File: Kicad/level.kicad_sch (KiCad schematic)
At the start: 38 parts, among them Q1 2N7002, Q10 MMBT5551L, Q11 2N7002, Q12 2N7002, Q2 2N7002, Q3 AO3401A, Q4 MMBT5551L, Q5 2N7002, Q6 2N7002, Q7 AO3401A, Q8 2N7002, Q9 2N7002, SW2 TEST_1, SW3 TEST_2

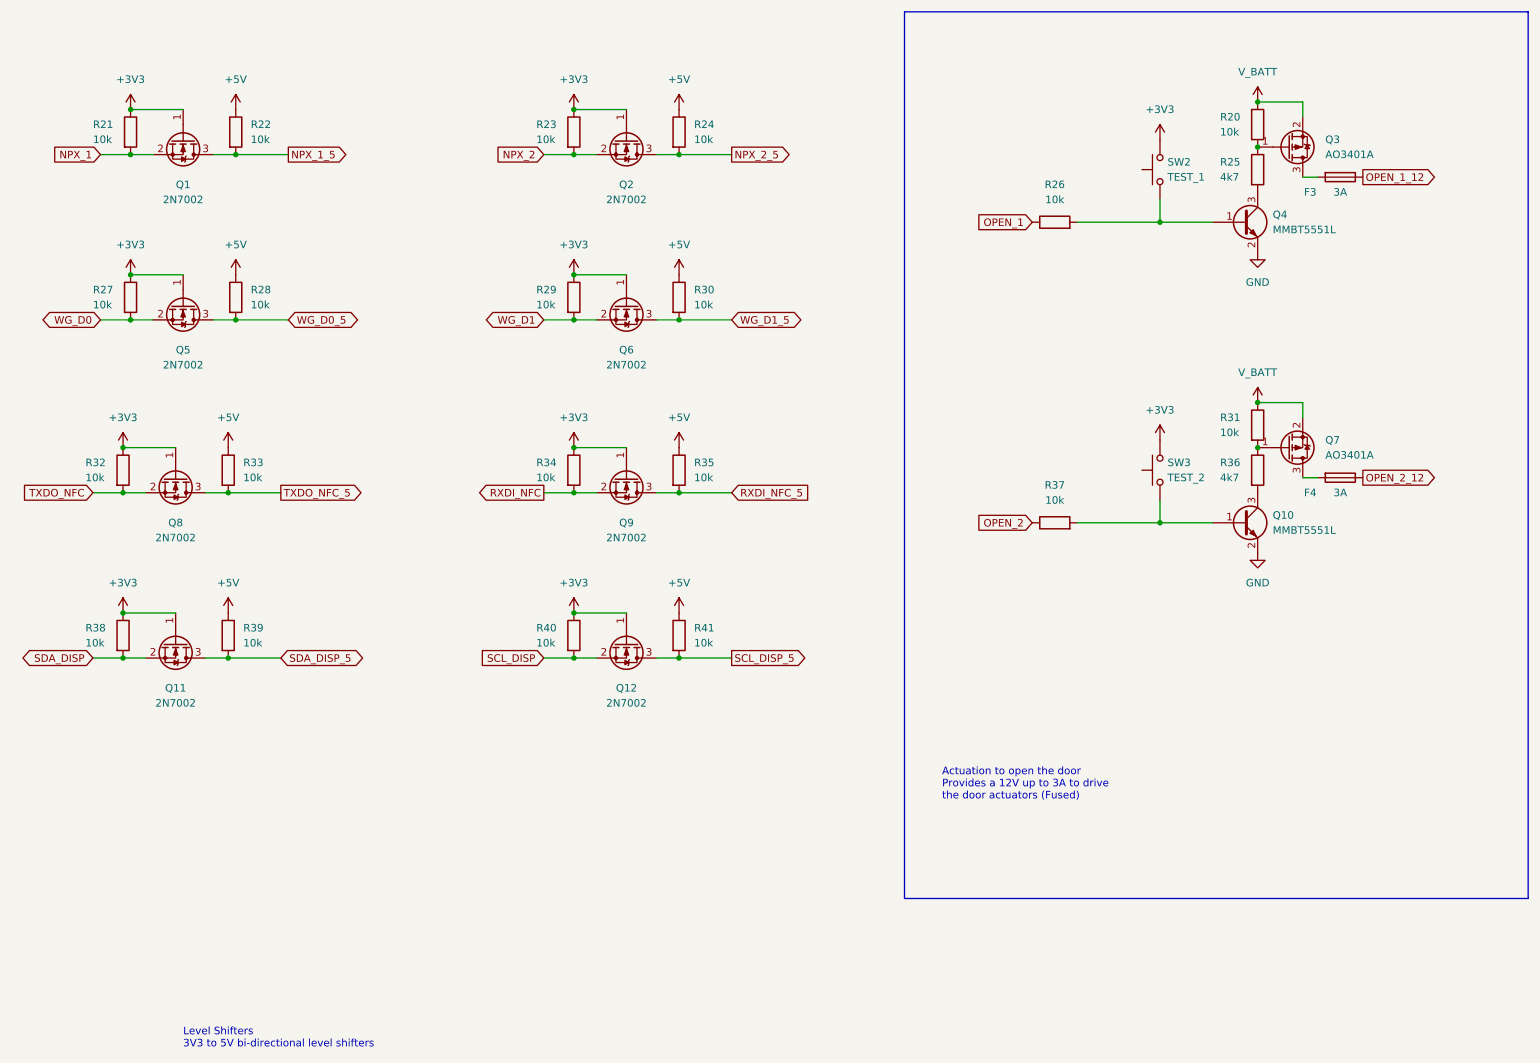
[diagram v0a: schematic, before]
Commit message: Rework of power circuits to improve protection
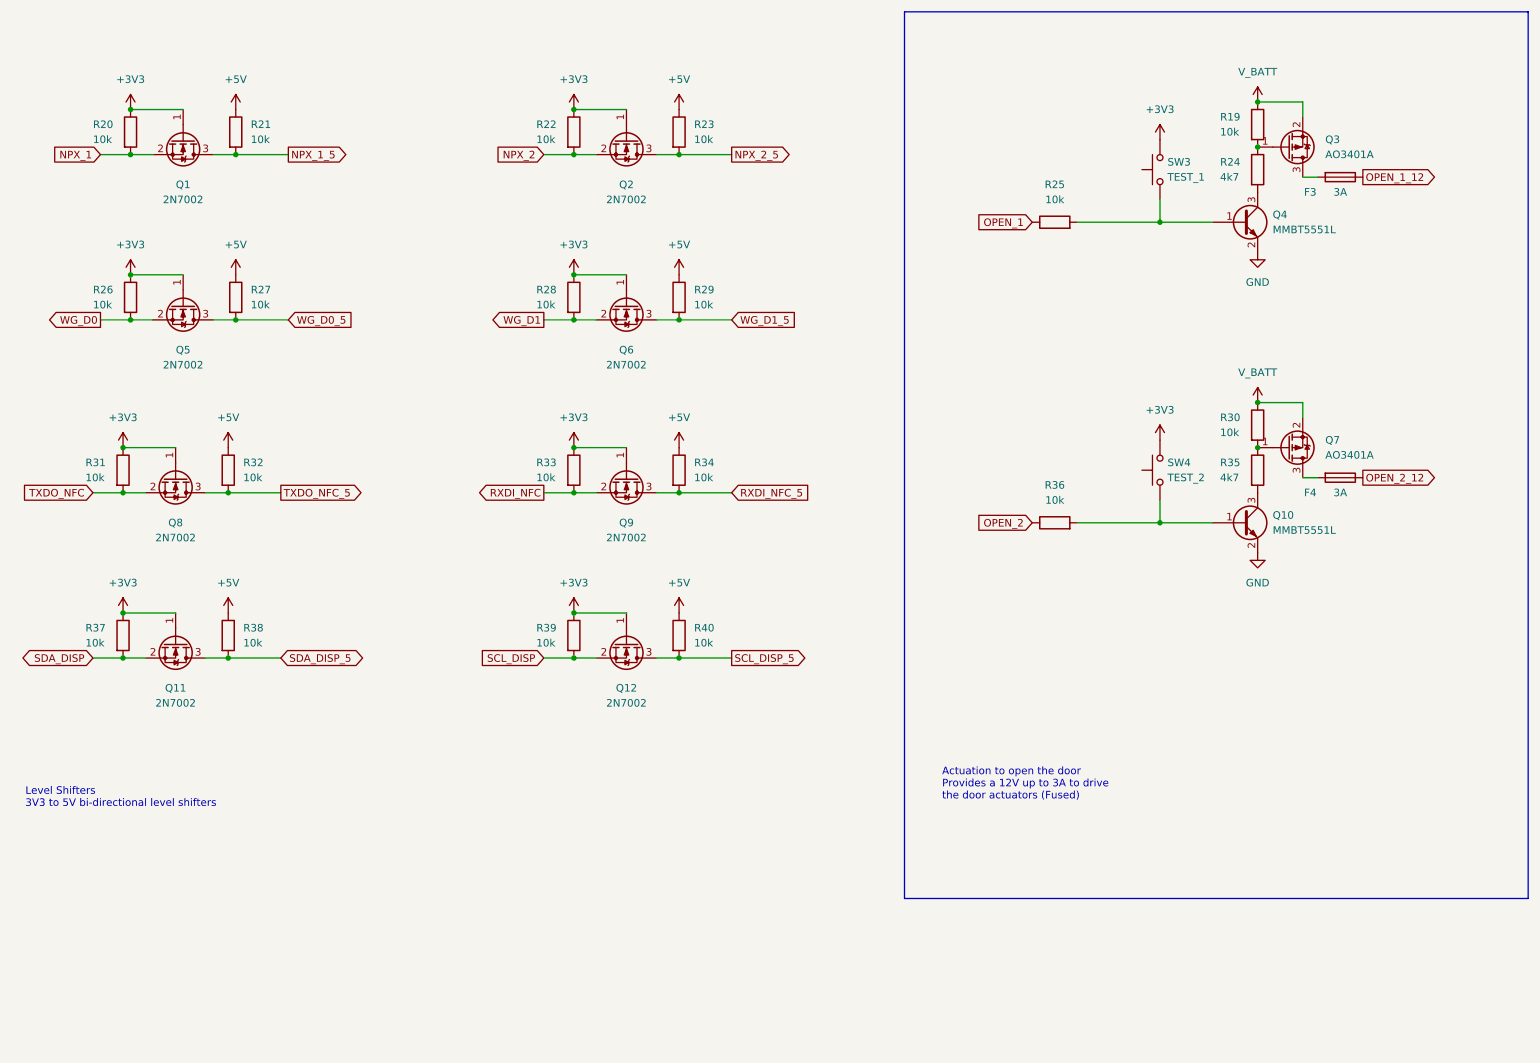
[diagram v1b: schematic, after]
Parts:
- renumbered R20 to R19, R21 to R20, R22 to R21, R23 to R22, R24 to R23, R25 to R24, R26 to R25, R27 to R26, R28 to R27, R29 to R28, R30 to R29, R31 to R30, R32 to R31, R33 to R32, R34 to R33, R35 to R34, R36 to R35, R37 to R36, R38 to R37, R39 to R38, R40 to R39, R41 to R40, SW2 to SW3, SW3 to SW4
